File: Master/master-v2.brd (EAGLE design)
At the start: 101.6 x 86.4 mm, 59 parts, among them J1 ISP, K1 653002114822, K2 653002114822, K3 653002114822, K4 653002114822, U1 ATMEGA128RFA1, U3 ULN2003ANE4, Y1 16MHz, Y2 32.768kHz

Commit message: changes to master-v2
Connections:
- removed net N$21: U$3.6
- removed net N$22: U$6.12
- removed net N$23: U$6.11
- removed net VDD: C12.+, U$2.3
- net 3.3V: now also C12.+, U$2.3
- net SCL: now also U$6.12
- net SDA: now also U$3.6, U$6.11
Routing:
- net VDD: track 6.17 -> 0.00 mm
- net 3.3V: track 219.1 -> 225.3 mm
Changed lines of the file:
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@@
 <signal name="SDA">
 <contactref element="U1" pad="26"/>
+<contactref element="U$3" pad="6"/>
+<contactref element="U$6" pad="11"/>
+<wire x1="61.39" y1="11.44" x2="55.13" y2="48.95" width="0" layer="19" extent="1-1"/>
+<wire x1="51.36" y1="9.99" x2="61.39" y2="11.44" width="0" layer="19" extent="1-1"/>
 </signal>
 <signal name="SCL">
 <contactref element="U1" pad="25"/>
 <contactref element="U$3" pad="4"/>
-<wire x1="50.41" y1="10.94" x2="55.63" y2="48.95" width="0" layer="19" extent="1-1"/>
+<contactref element="U$6" pad="12"/>
+<wire x1="61.39" y1="11.94" x2="55.63" y2="48.95" width="0" layer="19" extent="1-1"/>
+<wire x1="50.41" y1="10.94" x2="61.39" y2="11.94" width="0" layer="19" extent="1-1"/>
 </signal>
 <signal name="PB7">
@@
 <wire x1="43.1292" y1="22.86" x2="43.18" y2="22.86" width="0.254" layer="16"/>
 <via x="45.8724" y="20.1168" extent="1-16" drill="0.6096"/>
+<contactref element="U$2" pad="3"/>
+<contactref element="C12" pad="+"/>
+<wire x1="72.0852" y1="79.7052" x2="68.1228" y2="79.7052" width="0.254" layer="1"/>
+<wire x1="73.4568" y1="81.0768" x2="72.0852" y2="79.7052" width="0.254" layer="1"/>
+<wire x1="68.1228" y1="79.7052" x2="67.99" y2="79.66" width="0.254" layer="1"/>
+<wire x1="73.4568" y1="81.0768" x2="73.58" y2="81.11" width="0.254" layer="1"/>
+<wire x1="55.9308" y1="50.1904" x2="67.99" y2="79.66" width="0" layer="19" extent="1-1"/>
 </signal>
 <signal name="DTR">
@@
 <wire x1="32.9184" y1="78.6384" x2="33.02" y2="78.74" width="0.254" layer="1"/>
 </signal>
-<signal name="VDD">
-<contactref element="U$2" pad="3"/>
-<contactref element="C12" pad="+"/>
-<wire x1="72.0852" y1="79.7052" x2="68.1228" y2="79.7052" width="0.254" layer="1"/>
-<wire x1="73.4568" y1="81.0768" x2="72.0852" y2="79.7052" width="0.254" layer="1"/>
-<wire x1="68.1228" y1="79.7052" x2="67.99" y2="79.66" width="0.254" layer="1"/>
-<wire x1="73.4568" y1="81.0768" x2="73.58" y2="81.11" width="0.254" layer="1"/>
-</signal>
 <signal name="N$1">
 <contactref element="D1" pad="C"/>
@@
 <via x="49.6824" y="14.0208" extent="1-16" drill="0.6096"/>
 </signal>
-<signal name="N$21">
-<contactref element="U$3" pad="6"/>
-</signal>
-<signal name="N$22">
-<contactref element="U$6" pad="12"/>
-</signal>
-<signal name="N$23">
-<contactref element="U$6" pad="11"/>
-</signal>
 <signal name="N$29">

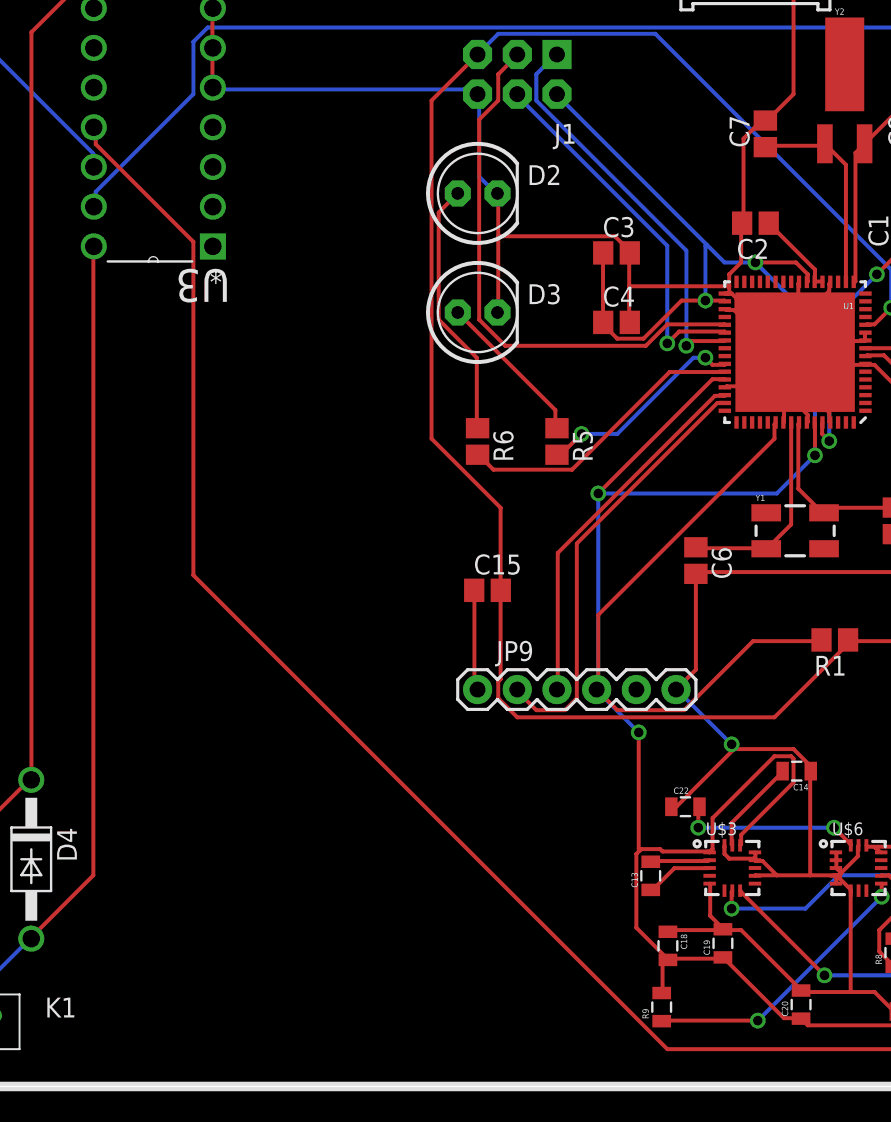
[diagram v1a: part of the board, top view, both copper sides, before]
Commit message: Change motor pins in master v2
Changed Pin enumeration for motors. There was one conflict with one Led
so it was changed to another pin. Also routing of those pins was done.
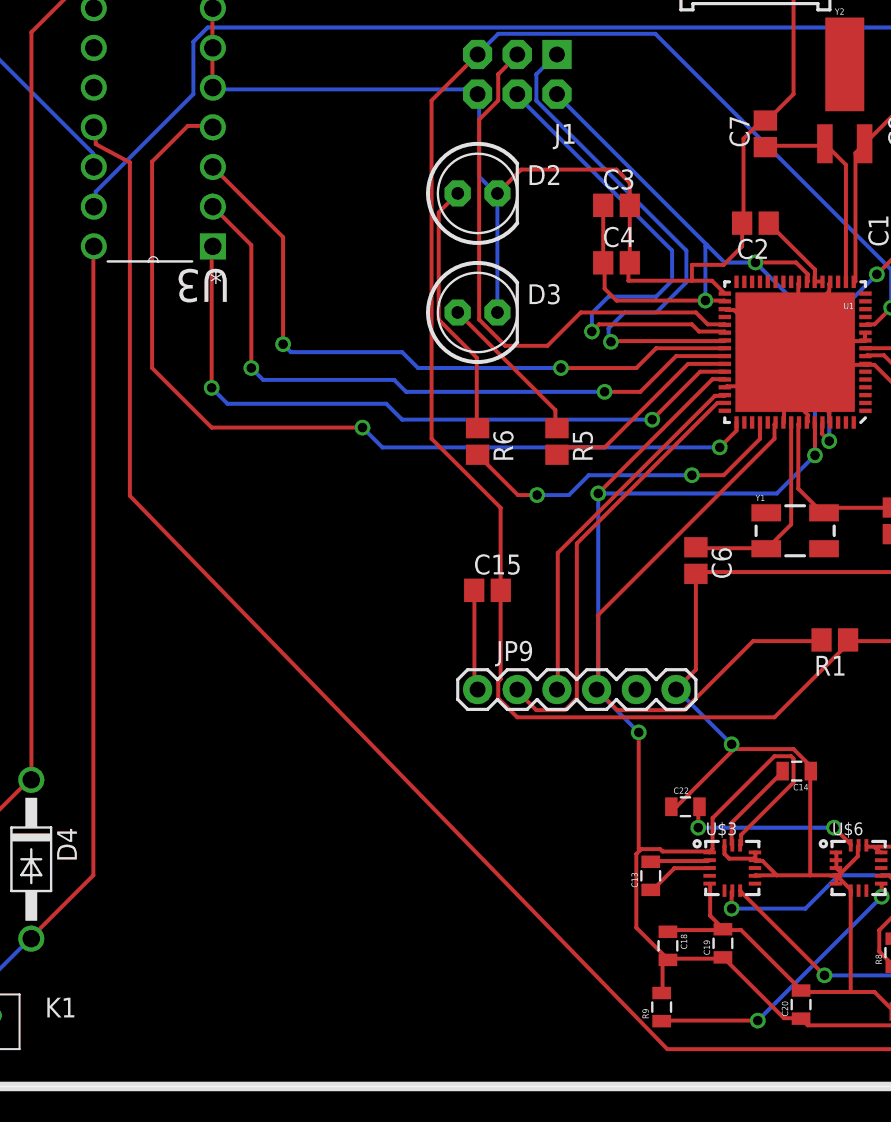
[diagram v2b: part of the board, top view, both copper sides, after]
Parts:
- moved C4 3.81 mm to (44.5, 50.2)
- moved C3 3.05 mm to (44.5, 53.8)
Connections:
- net PB4: now also U3.3; no longer U3.1
- net PB6: no longer U3.3
- net PB7: now also U3.1; no longer R6.2, U3.4
- net PE3: now also U3.4
- net PE6: now also R6.2
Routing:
- net PE3: track 0.00 -> 58.5 mm, vias 0 -> 2
- net PB5: track 0.00 -> 43.2 mm, vias 0 -> 2
- net PB4: track 0.00 -> 42.6 mm, vias 0 -> 2
- net PB7: track 18.8 -> 44.0 mm, vias 0 -> 2
- net PE6: track 0.00 -> 21.7 mm, vias 0 -> 2
- net MOSI: track 24.0 -> 32.1 mm
- net MISO: track 25.8 -> 33.6 mm
- net GND: track 356.6 -> 353.6 mm
- net SCK: track 35.0 -> 35.6 mm
- net PB6: track 13.6 -> 13.1 mm, vias 2 -> 0

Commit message: Adding Debug pins
Changed Motor pin numbers and added Debug pins in the schematic.
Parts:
- added JP4: Debug, SparkFun:1X02
- moved C2 7.09 mm to (49.1, 58.4), turned to 90 degrees
- moved JP3 1.52 mm to (33.0, 79.8)
- moved C19 0.25 mm to (51.3, 6.37)
- moved C18 0.25 mm to (47.7, 6.21)
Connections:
- net PB7: now also R6.2; no longer U3.1
- net PE4: now also U3.1
- net PE6: no longer R6.2
- net RX1: now also JP4.2
- net TX1: now also JP4.1
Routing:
- net SDA: track 0.00 -> 86.7 mm, vias 0 -> 3
- net SCL: track 0.00 -> 72.8 mm, vias 0 -> 3
- net 3.3V: track 224.9 -> 297.0 mm, vias 5 -> 6
- net PE4: track 0.00 -> 47.4 mm, vias 0 -> 2
- net TX1: track 0.00 -> 31.2 mm, vias 0 -> 2
- net RX1: track 0.00 -> 27.3 mm, vias 0 -> 2
- net PB7: track 44.0 -> 19.9 mm, vias 2 -> 0
- net PE6: track 21.7 -> 0.00 mm, vias 2 -> 0
- net RESET: track 116.8 -> 104.2 mm, vias 1 -> 2
- net DVDD: track 5.47 -> 16.4 mm
- net N$32: track 124.6 -> 130.7 mm
- net AVDD: track 15.8 -> 20.3 mm
- net VCC: track 292.6 -> 295.6 mm, vias 0 -> 1
- net N$18: track 18.2 -> 20.7 mm
- net GND: track 353.6 -> 351.2 mm
